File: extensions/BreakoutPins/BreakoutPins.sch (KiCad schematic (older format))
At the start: 7 parts, among them M1 MH_M3, M2 MH_M3, M3 MH_M3, M4 MH_M3, P1 Smoothie-teer-Daisy, P2 CONN_01X10, P3 Smoothie-teer-Daisy

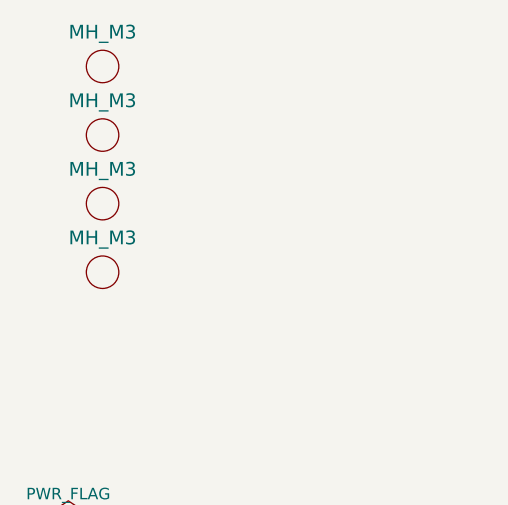
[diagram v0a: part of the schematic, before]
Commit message: Update to BreakoutPins
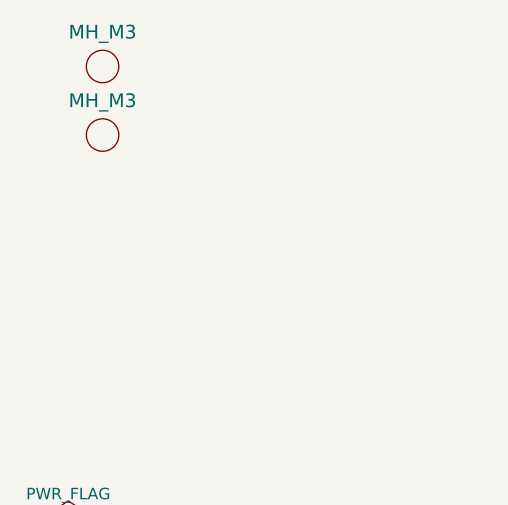
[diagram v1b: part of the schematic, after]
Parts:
- removed M3, M4: MH_M3, SBV2_Footprints:M3_Mounting_Hole, symbol MH
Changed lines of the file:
@@
-	1    0    0    -1
-$EndComp
-$Comp
-L MH M3
-U 1 1 5723E54E
-P 1100 1800
-F 0 "M3" H 1100 1650 60  0001 C CNN
-F 1 "MH_M3" H 1100 1950 60  0000 C CNN
-F 2 "SBV2_Footprints:M3_Mounting_Hole" H 1100 1800 60  0001 C CNN
-F 3 "" H 1100 1800 60  0000 C CNN
-F 4 "ND" H 1100 1800 60  0001 C CNN "Digikey Part No."
-F 5 "N/A" H -1700 -4200 60  0001 C CNN "DKPN"
-F 6 "N/A" H -1700 -4200 60  0001 C CNN "MFPN"
-	1    1100 1800
-	1    0    0    -1
-$EndComp
-$Comp
-L MH M4
-U 1 1 5723E55F
-P 1100 2100
-F 0 "M4" H 1100 1950 60  0001 C CNN
-F 1 "MH_M3" H 1100 2250 60  0000 C CNN
-F 2 "SBV2_Footprints:M3_Mounting_Hole" H 1100 2100 60  0001 C CNN
-F 3 "" H 1100 2100 60  0000 C CNN
-F 4 "ND" H 1100 2100 60  0001 C CNN "Digikey Part No."
-F 5 "N/A" H -1700 -3900 60  0001 C CNN "DKPN"
-F 6 "N/A" H -1700 -3900 60  0001 C CNN "MFPN"
-	1    1100 2100
 	1    0    0    -1
 $EndComp

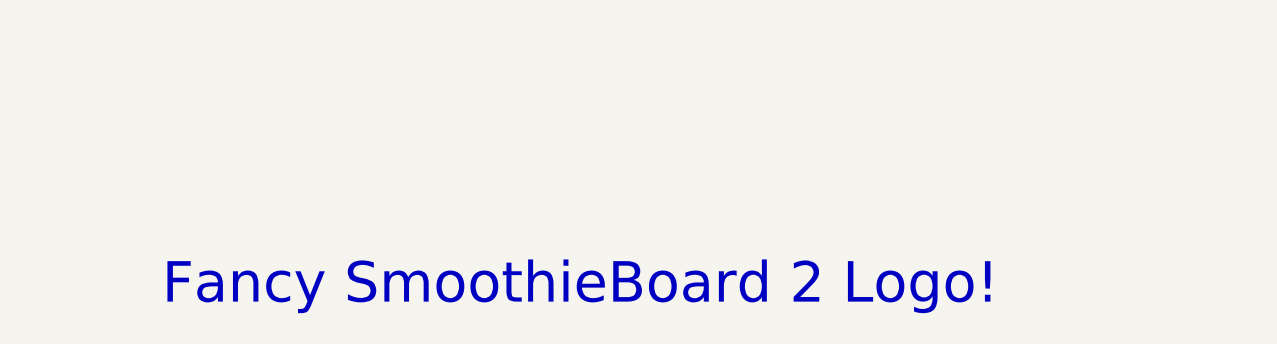
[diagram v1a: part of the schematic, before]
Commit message: Corrected part number for gadgeteer connectors; update libraries; add some doc files
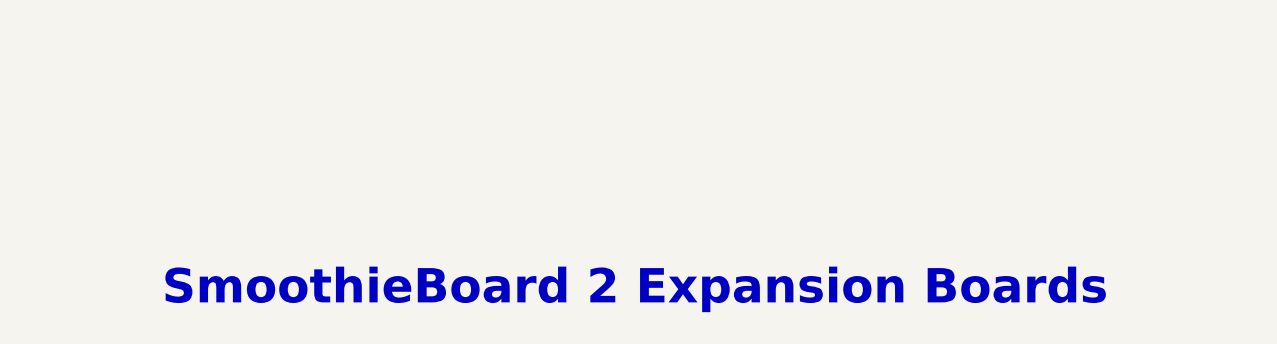
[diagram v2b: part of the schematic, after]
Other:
- note added: "SmoothieBoard 2 Expansion Boards"
- note removed: "Fancy SmoothieBoard 2 Logo!"
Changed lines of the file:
@@
 	1    0    0    -1
 $EndComp
-Text Notes 7100 6900 0    177  ~ 0
-Fancy SmoothieBoard 2 Logo!
+Text Notes 7100 6900 0    150  ~ 30
+SmoothieBoard 2 Expansion Boards
 $Comp
 L CONN_01X10 P2
